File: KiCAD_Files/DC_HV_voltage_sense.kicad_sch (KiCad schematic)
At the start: 16 parts, among them U401 AMC1311BDWVR, U402 MCP6486UT-E/LT

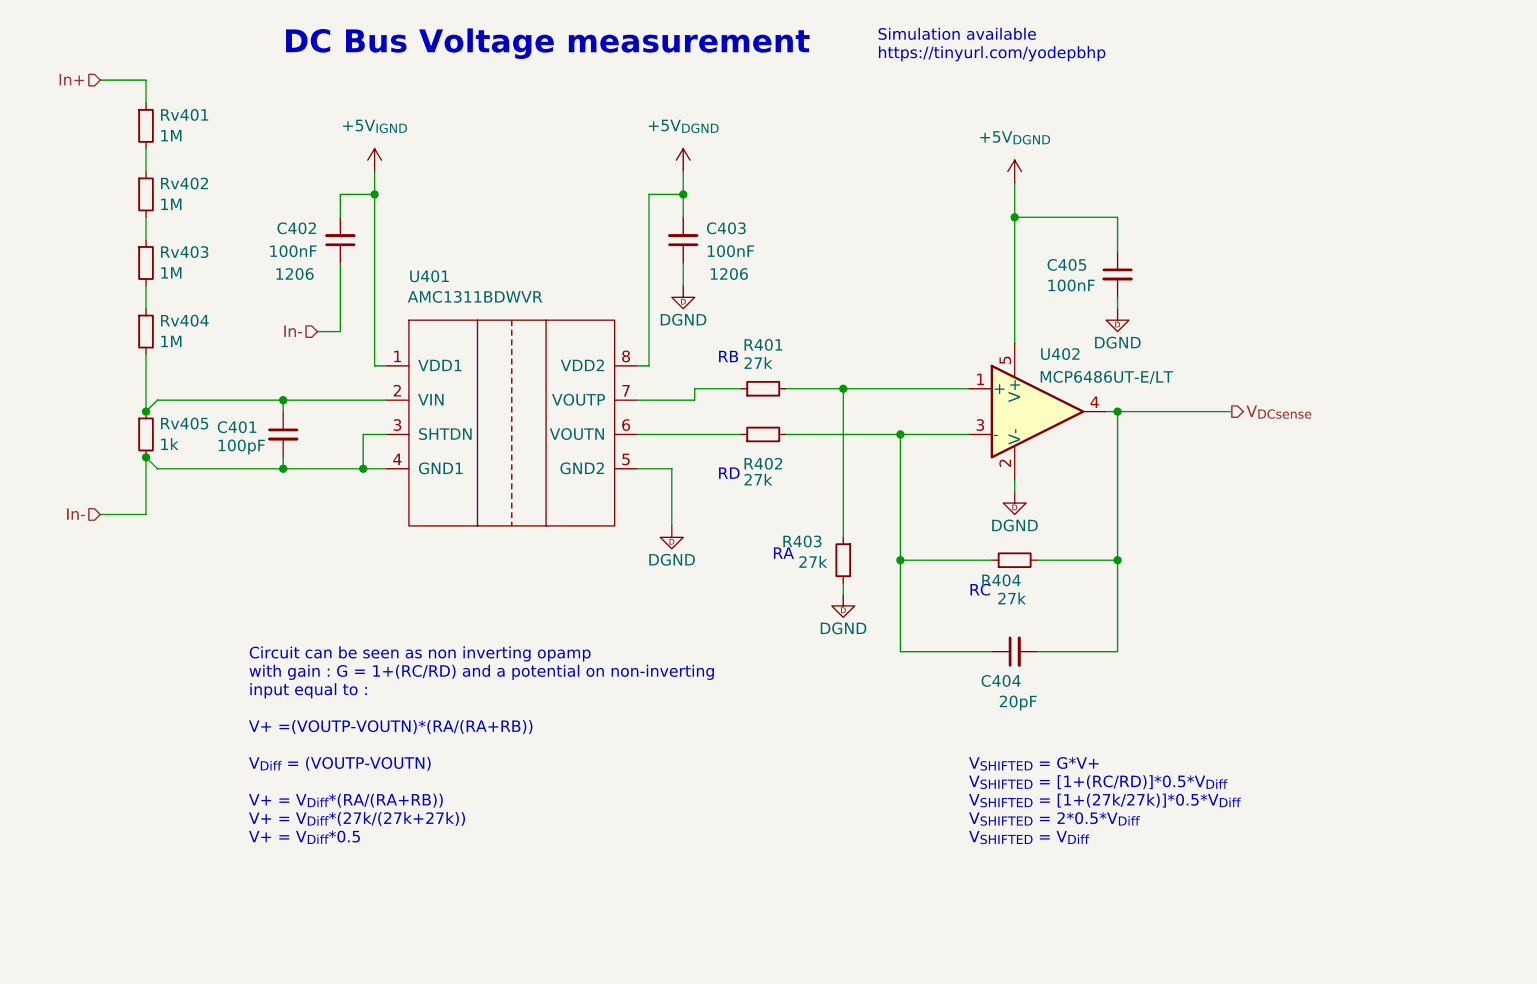
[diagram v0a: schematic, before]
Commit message: First routing pass complete.
Signed-off-by: Jean Alinei <jean.alinei@owntech.org>
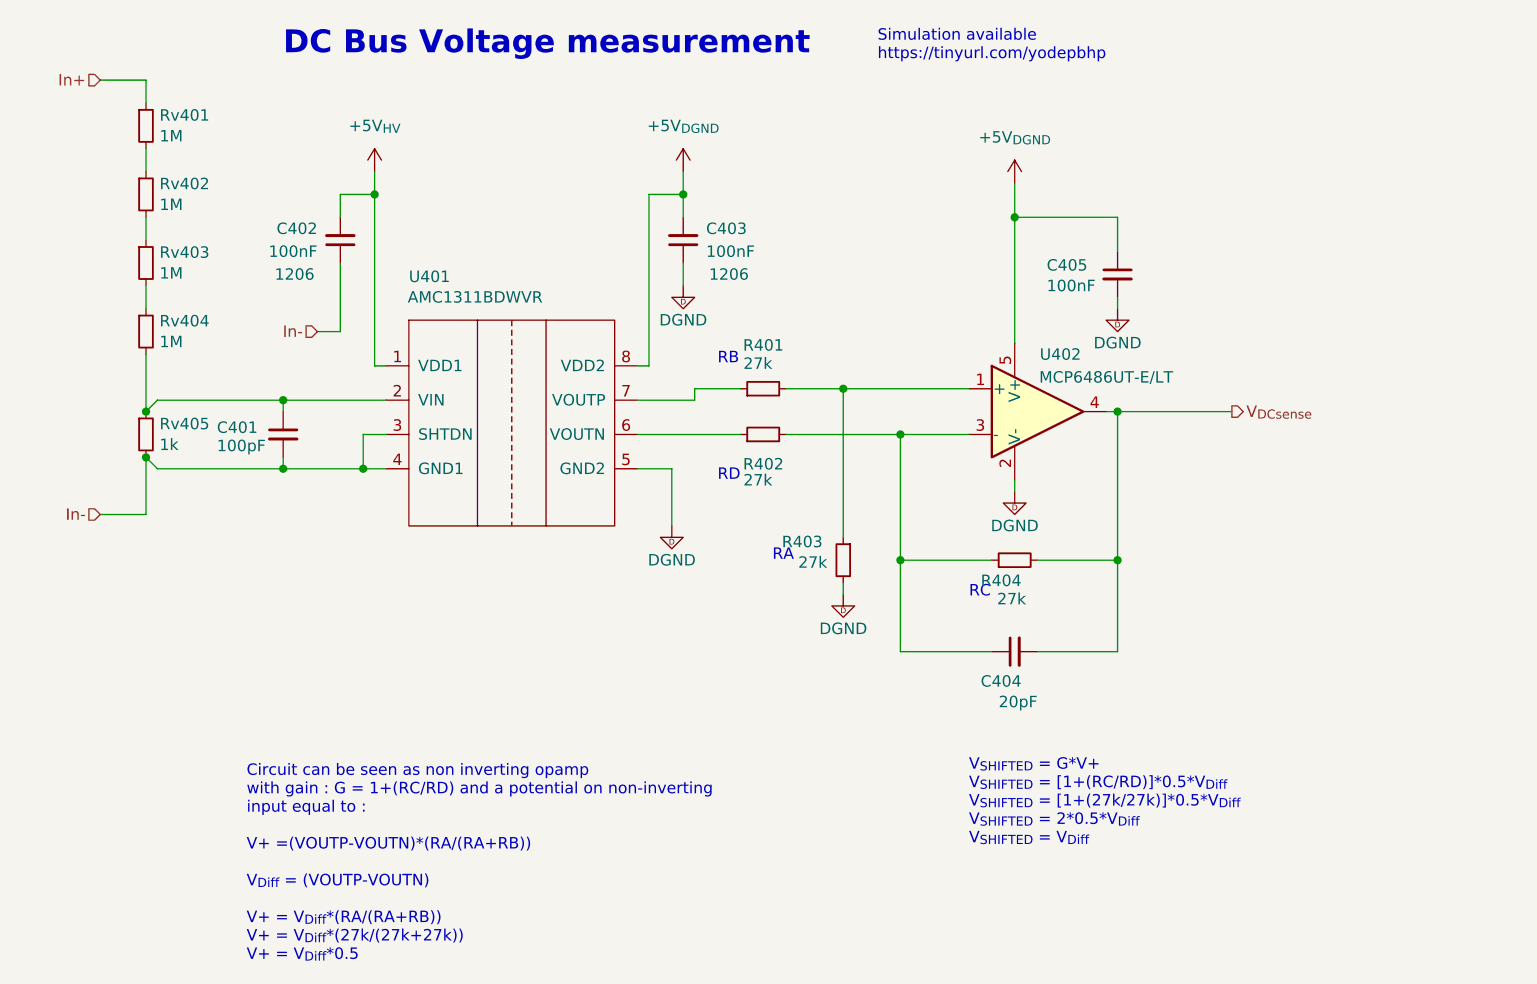
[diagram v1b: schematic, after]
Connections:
- net +5V_{IGND} renamed +5V_{HV}
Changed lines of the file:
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@@
 	(text "Circuit can be seen as non inverting opamp\nwith gain : G = 1+(RC/RD) and a potential on non-inverting\ninput equal to :\n\nV+ =(VOUTP-VOUTN)*(RA/(RA+RB))\n\nV_{Diff} = (VOUTP-VOUTN)\n\nV+ = V_{Diff}*(RA/(RA+RB))\nV+ = V_{Diff}*(27k/(27k+27k))\nV+ = V_{Diff}*0.5"
 		(exclude_from_sim no)
-		(at 44.45 137.16 0)
+		(at 44.196 150.114 0)
 		(effects
 			(font
@@
 			)
 			(justify right)
+		)
+	)
+	(rule_area
+		(polyline
+			(pts
+				(xy 73.66 52.07) (xy 73.66 124.46) (xy 168.91 124.46) (xy 168.91 52.07)
+			)
+			(stroke
+				(width 0)
+				(type dash)
+			)
+			(fill
+				(type none)
+			)
+		)
+	)
+	(netclass_flag ""
+		(length 2.54)
+		(shape round)
+		(at 83.82 124.46 0)
+		(fields_autoplaced yes)
+		(effects
+			(font
+				(size 1.27 1.27)
+			)
+			(justify left bottom)
+		)
+		(property "Netclass" "DGND"
+			(at 84.5185 121.92 0)
+			(effects
+				(font
+					(size 1.27 1.27)
+				)
+				(justify left)
+			)
+		)
+		(property "Component Class" ""
+			(at -175.26 76.2 0)
+			(effects
+				(font
+					(size 1.27 1.27)
+					(italic yes)
+				)
+				(hide yes)
+			)
 		)
 	)
@@
 			)
 		)
-		(property "Datasheet" "${KIPRJMOD}\\datasheets\\amc1311.pdf"
+		(property "Datasheet" "./datasheets/amc1311.pdf"
 			(at 102.87 71.12 0)
 			(effects
@@
 			)
 		)
-		(property "Value" "+5V_{IGND}"
+		(property "Value" "+5V_{HV}"
 			(at 58.42 57.15 0)
 			(effects

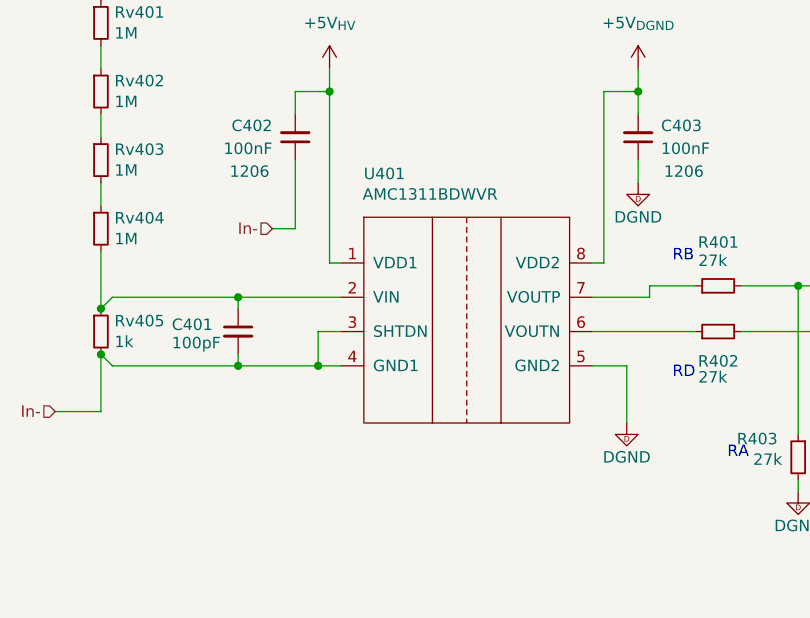
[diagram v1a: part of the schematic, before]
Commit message: Added DRC rules according to IEC60664 and IPC2221.
Signed-off-by: Jean Alinei <jean.alinei@owntech.org>
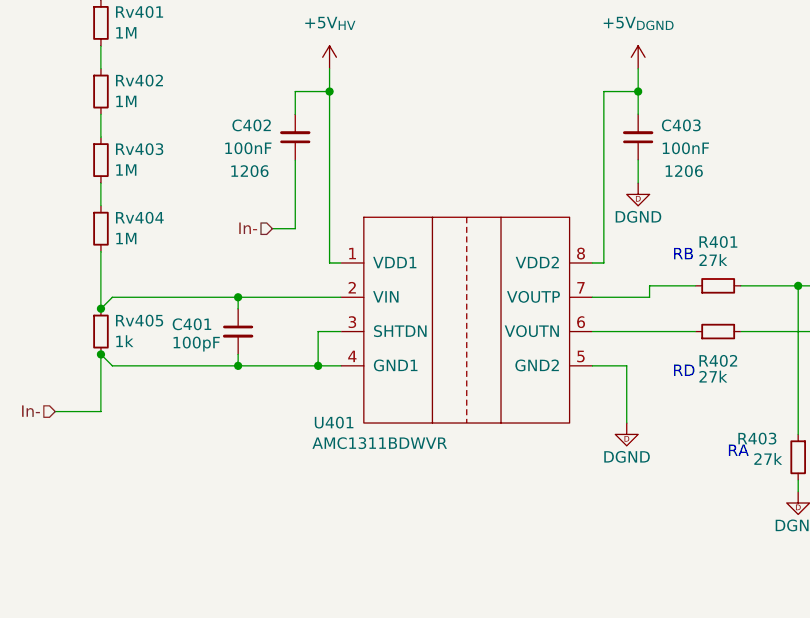
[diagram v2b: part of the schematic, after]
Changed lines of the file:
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@@
 		(polyline
 			(pts
-				(xy 73.66 52.07) (xy 73.66 124.46) (xy 168.91 124.46) (xy 168.91 52.07)
+				(xy 76.2 52.07) (xy 76.2 124.46) (xy 168.91 124.46) (xy 168.91 52.07)
+			)
+			(stroke
+				(width 0)
+				(type dash)
+			)
+			(fill
+				(type none)
+			)
+		)
+	)
+	(rule_area
+		(polyline
+			(pts
+				(xy 71.12 124.46) (xy 71.12 52.07) (xy 45.72 52.07) (xy 40.64 57.15) (xy 17.78 57.15) (xy 17.78 124.46)
 			)
 			(stroke
@@
 		(property "Component Class" ""
 			(at -175.26 76.2 0)
+			(effects
+				(font
+					(size 1.27 1.27)
+					(italic yes)
+				)
+				(hide yes)
+			)
+		)
+	)
+	(netclass_flag ""
+		(length 2.54)
+		(shape round)
+		(at 40.64 124.46 0)
+		(fields_autoplaced yes)
+		(effects
+			(font
+				(size 1.27 1.27)
+			)
+			(justify left bottom)
+		)
+		(property "Netclass" "GND_HV"
+			(at 41.3385 121.92 0)
+			(effects
+				(font
+					(size 1.27 1.27)
+				)
+				(justify left)
+			)
+		)
+		(property "Component Class" ""
+			(at -218.44 76.2 0)
 			(effects
 				(font
@@
 		(dnp no)
 		(property "Reference" "U401"
-			(at 64.516 73.914 0)
+			(at 58.928 101.6 0)
 			(effects
 				(font
@@
 		)
 		(property "Value" "AMC1311BDWVR"
-			(at 69.596 76.2 0)
-			(effects
-				(font
+			(at 64.008 103.886 0)
+			(effects
+				(font

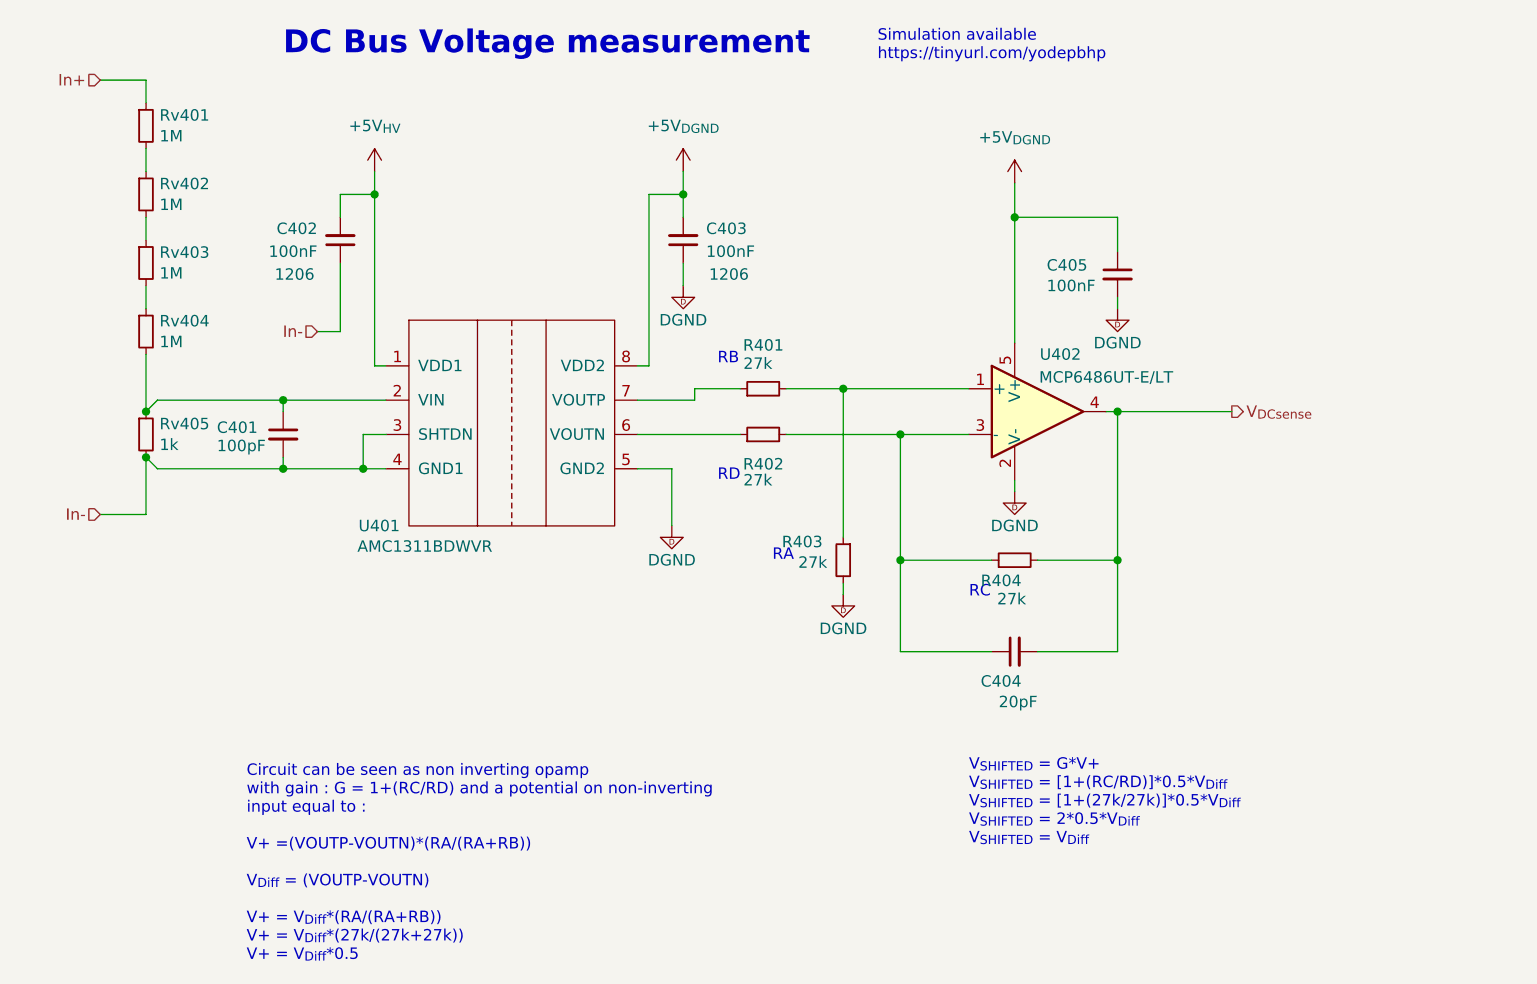
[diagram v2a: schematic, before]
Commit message: Added passive references. Added ESD protection for MCU pins.
Signed-off-by: Jean Alinei <jean.alinei@owntech.org>
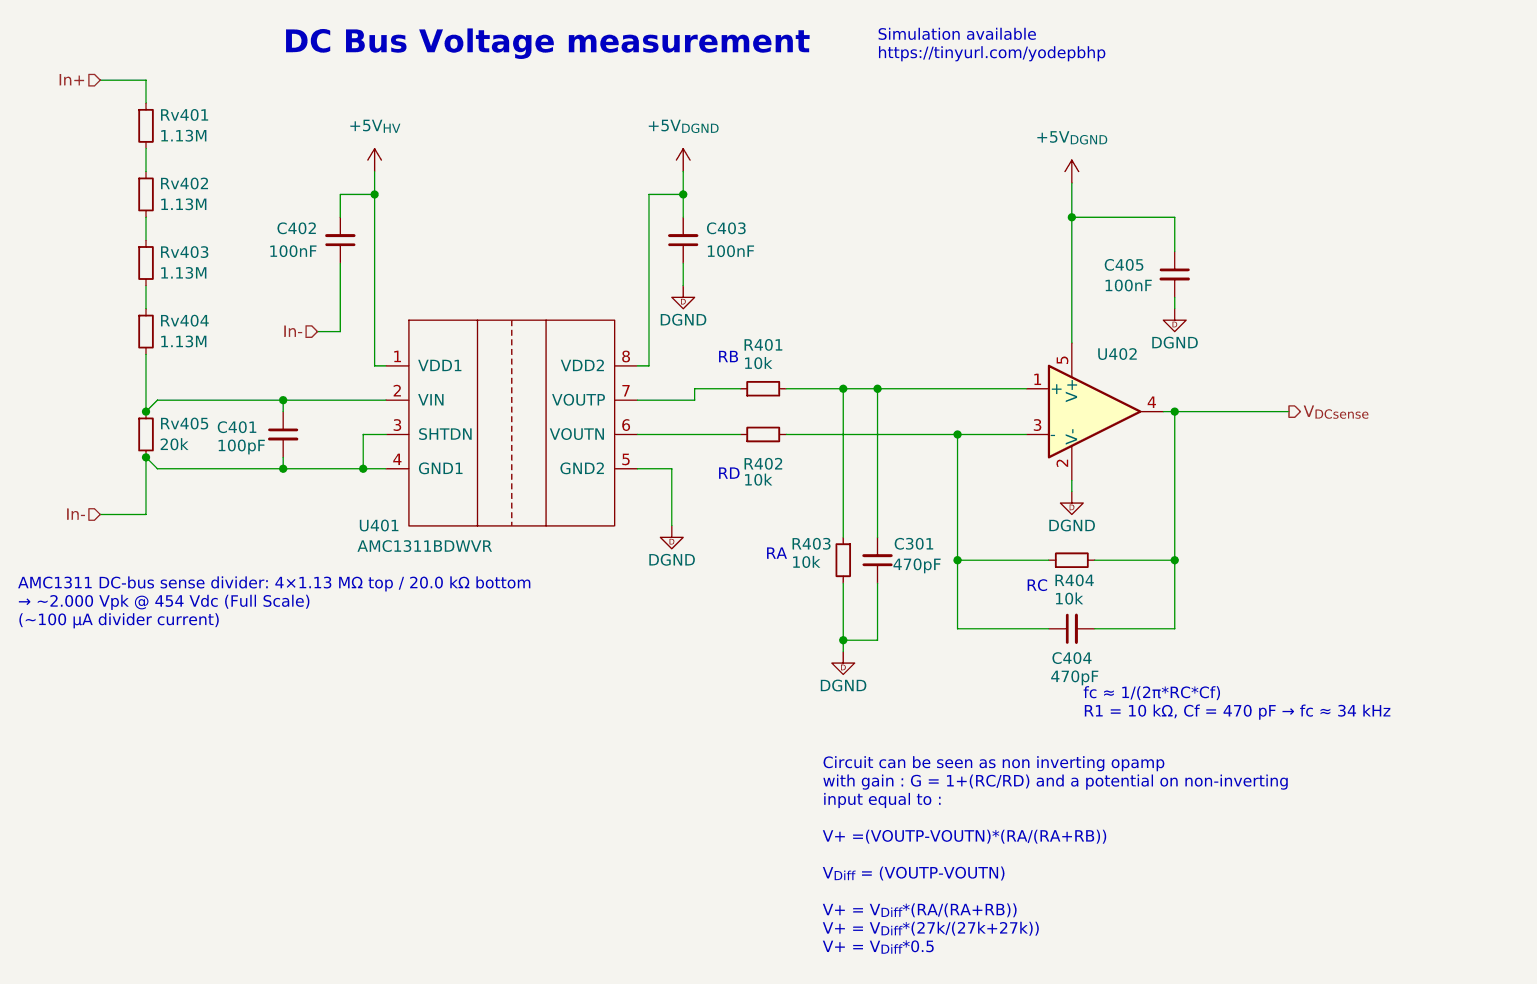
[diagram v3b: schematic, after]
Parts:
- added C301: 470pF, Footprints:C_0805_2012Metric, symbol Device:C_Small
- C401: Dielectric NP0 -> (none); LCSC (none) -> C1790; Package 0805 -> (none); Voltage 50V -> (none); manf# CC0805JRNPO9BN200 -> (none)
- C402, C403: Dielectric X7R -> (none); LCSC C5449000 -> C24497; Metal content BaTiO3 -> (none); Package 1206 -> (none); Subfunction VIHigh measure -> (none); Voltage 50V -> (none); manf# C1206C104K5RAC7867 -> (none)
- C404: value 20pF -> 470pF; Dielectric NP0 -> (none); LCSC (none) -> C1743; Package 0805 -> (none); Voltage 50V -> (none); manf# CC0805JRNPO9BN200 -> (none)
- C405: Dielectric X7R -> (none); LCSC C5449000 -> C49678; Package 1206 -> (none); Voltage 50V -> (none); manf# C1206C104K5RAC7867 -> (none)
- R401, R402, R403, R404: value 27k -> 10k; LCSC (none) -> C17414; Package 0805 -> (none); Technology Thin film -> (none); manf# RT0805DRD0727KL -> (none)
- Rv401, Rv402, Rv403, Rv404: value 1M -> 1.13M; LCSC (none) -> C2091141
- Rv405: value 1k -> 20k; LCSC (none) -> C4328
- U401: manf# AMC1311BDWVR -> (none)
- U402: Rotation Offset (none) -> 90; Subfunction IILow Measure -> (none); manf# MCP6486UT-E/LT -> (none)
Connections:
- net DGND: now also C301.1
- net at R401.2, R403.1, U402.1 (+): now also C301.2
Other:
- note added: "AMC1311 DC-bus sense divider: 4×1.13 MΩ top / 20.0 kΩ bottom → ~2.000 Vpk @ 454 Vdc (Full Scale) (~100 µA divider current)"
- note added: "fc ​≈ 1/(2π*RC*Cf)​ R1 = 10 kΩ, Cf = 470 pF → fc ≈ 34 kHz"
- note removed: "V_{SHIFTED} = G*V+ V_{SHIFTED} = [1+(RC/RD)]*0.5*V_{Diff} V_{SHIFTED} = [1+(27k/27k)]*0.5*V_{Diff} V_{SHIFTED} = 2*0.5*V_{Diff} V_{SHIFTED} = V_{Diff}"
- moved on the sheet: C404, C405, R404, U402
